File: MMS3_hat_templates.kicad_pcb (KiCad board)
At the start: 2 copper layers, 100 x 50 mm, 69 parts, among them J1 Chainbus in, J10 Conn_01x02_Socket, J11 Conn_01x02_Socket, J12 Conn_01x02_Socket, J13 Conn_01x02_Socket, J2 Chainbus Out, J3 Conn_01x04_Pin, J6 Conn_01x02_Socket, J7 Conn_01x02_Socket, J8 Conn_01x02_Socket, J9 Conn_01x02_Socket, U1 SN74CB3Q3245PWR, U13 AMS1117, U14 TCA9535PWR_C130204, U16 MAX31855KASA+T, U17 MAX31855KASA+T, U18 MAX31855KASA+T, U19 MAX31855KASA+T, U2 M24C64, U20 MAX31855KASA+T, U21 MAX31855KASA+T, U22 MAX31855KASA+T, U5 MAX31855KASA+T

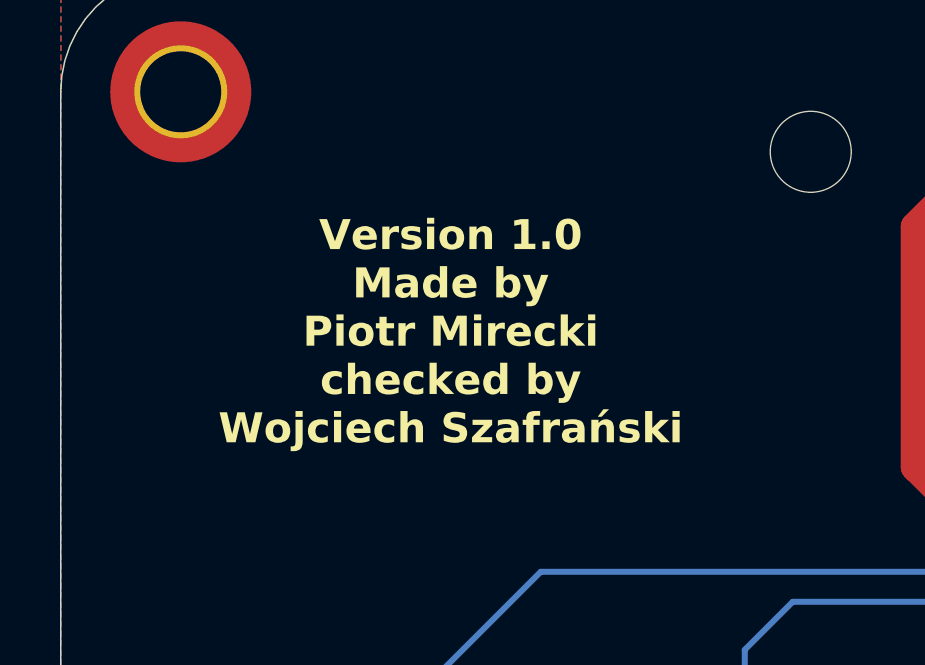
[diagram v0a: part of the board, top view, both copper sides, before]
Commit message: updated silkscreen
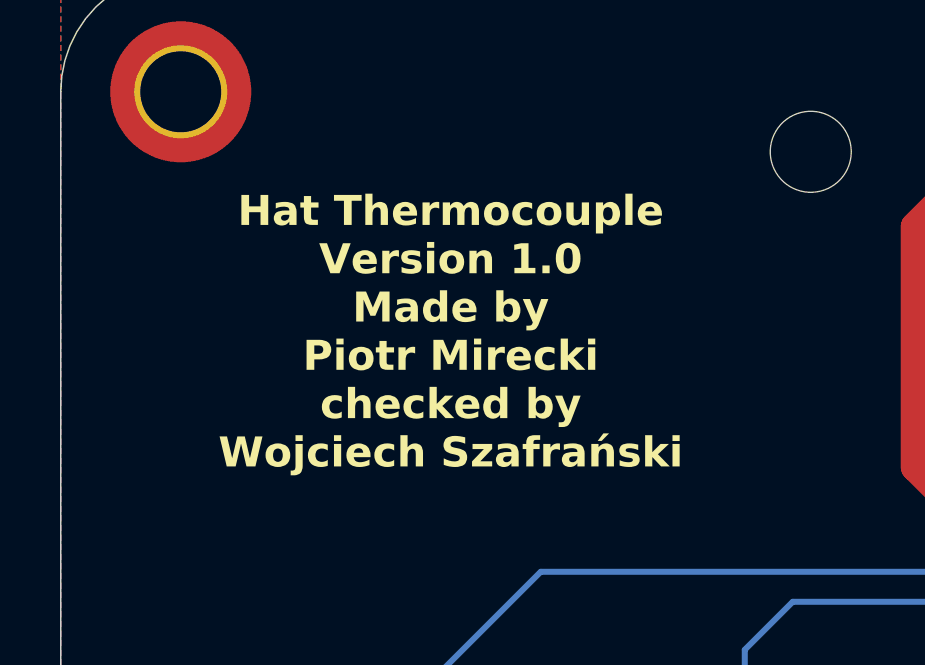
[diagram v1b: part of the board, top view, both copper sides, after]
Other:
- board text added: "Hat Thermocouple Version 1.0 Made by Piotr Mirecki checked by Wojciech Szafrański"
- board text removed: "Version 1.0 Made by Piotr Mirecki checked by Wojciech Szafrański"
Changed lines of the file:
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@@
 	(paper "A4")
 	(title_block
-		(title "MMS3 Hat Stepper Controler")
-		(date "2026-02-25")
-		(rev "R0")
-		(comment 1 "Made by Wojciech Szafrański")
+		(title "MMS3 Hat Thermocouple")
+		(date "2026-04-25")
+		(rev "V1.0")
+		(comment 1 "Made by Piotr Mirecki & Wojciech Szafrański")
 		(comment 2 "Designed in poland")
 		(comment 3 "MMS3 Hat based on Chainbus")
@@
 		)
 	)
-	(gr_text "Version 1.0\nMade by\nPiotr Mirecki\nchecked by\nWojciech Szafrański"
+	(gr_text "Hat Thermocouple\nVersion 1.0\nMade by\nPiotr Mirecki\nchecked by\nWojciech Szafrański"
 		(at 91 100 0)
 		(layer "F.SilkS")
